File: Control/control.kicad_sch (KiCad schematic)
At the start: 0 parts

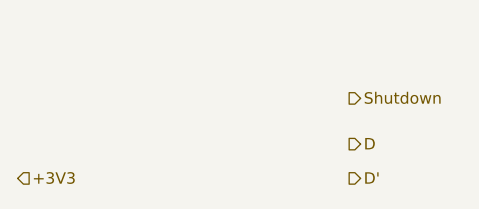
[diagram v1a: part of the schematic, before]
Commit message: added symbol libraries and finished gate driver circuitry schematic
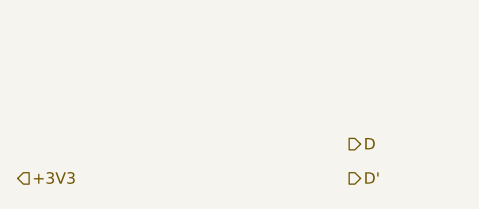
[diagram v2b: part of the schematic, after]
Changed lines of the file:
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@@
-		)
-	)
-	(hierarchical_label "Shutdown"
-		(shape output)
-		(at 176.53 90.17 0)
-		(effects
-			(font
-				(size 1.27 1.27)
-			)
-			(justify left)
 		)
 	)

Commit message: MSPM0 Connections
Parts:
- added J2-J4, J3-J1: Conn_01x10, Connector_PinSocket_2.54mm:PinSocket_2x10_P2.54mm_Vertical, symbol Connector_Generic:Conn_02x10_Odd_Even
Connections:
- net +3V3: now also J3-J1.1 (Pin_1)
- new net *D19: J2-J4.4 (Pin_4)
- new net *D37: J2-J4.7 (Pin_7)
- new net *D38: J2-J4.5 (Pin_5)
- new net *D39: J2-J4.3 (Pin_3)
- new net *D40: J2-J4.1 (Pin_1)
- new net +5V: J3-J1.2 (Pin_2)
- new net D10/SDA: J3-J1.19 (Pin_19)
- new net D11: J2-J4.20 (Pin_20)
- new net D12/SPI.CS: J2-J4.18 (Pin_18)
- new net D13/SPI.CS: J2-J4.16 (Pin_16)
- new net D14/SPI.MISO: J2-J4.14 (Pin_14)
- new net D15/SPI.MOSI: J2-J4.12 (Pin_12)
- new net D17: J2-J4.8 (Pin_8)
- new net D18/SPI.CS: J2-J4.6 (Pin_6)
- new net D23/ADC: J3-J1.6 (Pin_6)
- new net D24/ADC: J3-J1.8 (Pin_8)
- new net D25/ADC: J3-J1.10 (Pin_10)
- new net D26/ADC: J3-J1.12 (Pin_12)
- new net D27/ADC: J3-J1.14 (Pin_14)
- new net D28/ADC: J3-J1.16 (Pin_16)
- new net D29/DAC: J3-J1.18 (Pin_18)
- new net D2/ADC: J3-J1.3 (Pin_3)
- new net D30/DAC: J3-J1.20 (Pin_20)
- new net D31: J2-J4.19 (Pin_19)
- new net D32: J2-J4.17 (Pin_17)
- new net D33: J2-J4.15 (Pin_15)
- new net D34: J2-J4.13 (Pin_13)
- new net D35/TC: J2-J4.11 (Pin_11)
- new net D36/TC: J2-J4.9 (Pin_9)
- new net D3/UART.RX: J3-J1.5 (Pin_5)
- new net D4/UART.TX: J3-J1.7 (Pin_7)
- new net D5: J3-J1.9 (Pin_9)
- new net D6/ADC: J3-J1.11 (Pin_11)
- new net D7/SPI.CLK: J3-J1.13 (Pin_13)
- new net D8: J3-J1.15 (Pin_15)
- new net D9/SCL: J3-J1.17 (Pin_17)
- new net GND: J2-J4.2 (Pin_2), J3-J1.4 (Pin_4)
- new net RST/D16: J2-J4.10 (Pin_10)
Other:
- note added: "Distance between the two connection columns pins should be 1800 mil from the middle portion of the outer pins. Distance between the pins in the column is 100 mil."
- note added: "Page 5 of the documentation"
- note added: "Pin Schematics"

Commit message: Diff Amp
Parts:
- added R1, R2: 1000, Resistor_SMD:R_0603_1608Metric_Pad0.98x0.95mm_HandSolder, symbol Device:R_Small_US
- added R3, R4: 1100, Resistor_SMD:R_0603_1608Metric_Pad0.98x0.95mm_HandSolder, symbol Device:R_Small_US
- added U1: TLV2372, Package_SO:SOIC-8_3.9x4.9mm_P1.27mm, symbol Amplifier_Operational:TLV2372
- renumbered J2-J4 to J2-J?, J3-J1 to J3-J?
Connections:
- net +3V3: now also U1.8 (V+)
- net GND: now also R3.2, U1.4 (V-)
- new net: R2.2, R3.1, U1.2 (-)
- new net: R1.2, R4.1, U1.3 (+)
- new net V_{cap+}: R1.1
- new net V_{cap-}: R2.1
- new net Vout: R4.2, U1.1
- no-connect marks 0 -> 3
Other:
- note added: "Differential Amplifier V_{out}= 1.1(V_{cap-}-V_{cap+})"

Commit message: more simulation work + fixed some things in root schematic
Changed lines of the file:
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@@
 		)
 	)
-	(hierarchical_label "D"
+	(hierarchical_label "D1"
 		(shape output)
 		(at 176.53 95.25 0)
+		(effects
+			(font
+				(size 1.27 1.27)
+			)
+			(justify left)
+		)
+	)
+	(hierarchical_label "D2'"
+		(shape output)
+		(at 176.53 106.68 0)
 		(effects
 			(font
@@
 		)
 	)
-	(hierarchical_label "SCL_{IN}"
-		(shape input)
-		(at 161.29 95.25 180)
-		(effects
-			(font
-				(size 1.27 1.27)
-			)
-			(justify right)
-		)
-	)
 	(hierarchical_label "V_{cap-}"
 		(shape bidirectional)
@@
 		)
 	)
-	(hierarchical_label "SDA_{IN}"
-		(shape bidirectional)
-		(at 161.29 97.79 180)
-		(effects
-			(font
-				(size 1.27 1.27)
-			)
-			(justify right)
-		)
-	)
-	(hierarchical_label "D'"
+	(hierarchical_label "D1'"
 		(shape output)
 		(at 176.53 99.06 0)
@@
 		)
 	)
+	(hierarchical_label "D2"
+		(shape output)
+		(at 176.53 102.87 0)
+		(effects
+			(font
+				(size 1.27 1.27)
+			)
+			(justify left)
+		)
+	)

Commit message: wiring connected, now only need msmp0 pinout and footprint assignments
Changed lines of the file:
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@@
 	)
 	(hierarchical_label "V_{cap-}"
-		(shape bidirectional)
+		(shape input)
 		(at 118.11 77.47 180)
 		(effects
@@
 	)
 	(hierarchical_label "V_{cap+}"
-		(shape bidirectional)
+		(shape input)
 		(at 118.11 72.39 180)
 		(effects

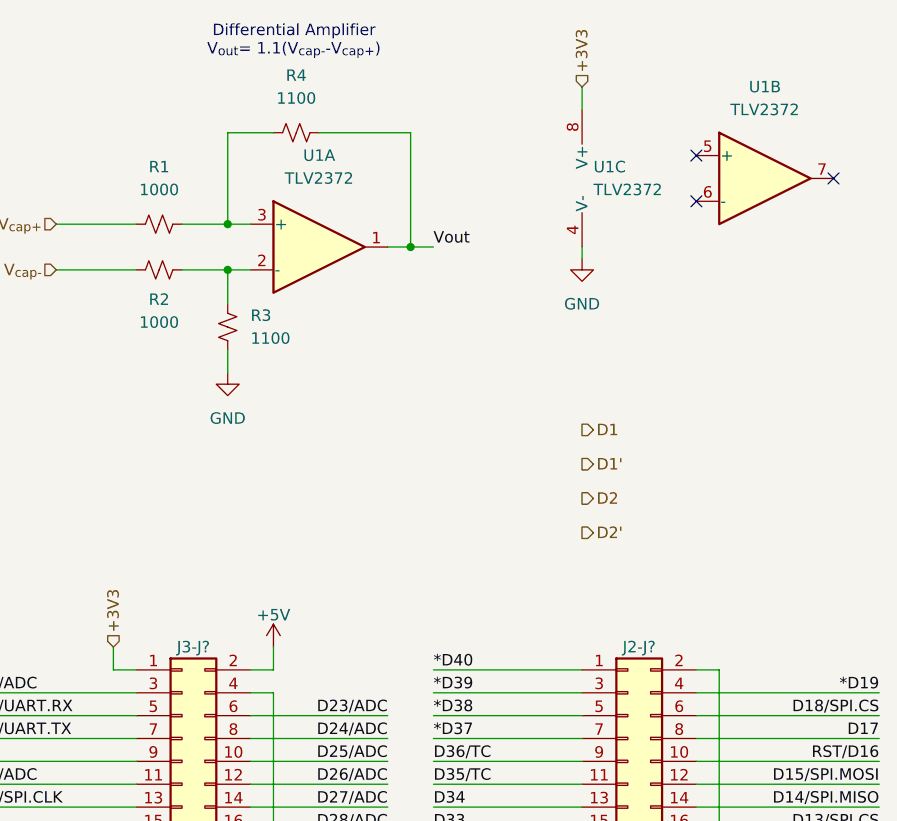
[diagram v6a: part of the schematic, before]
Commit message: removed v1 files and assigned mouser part numbers
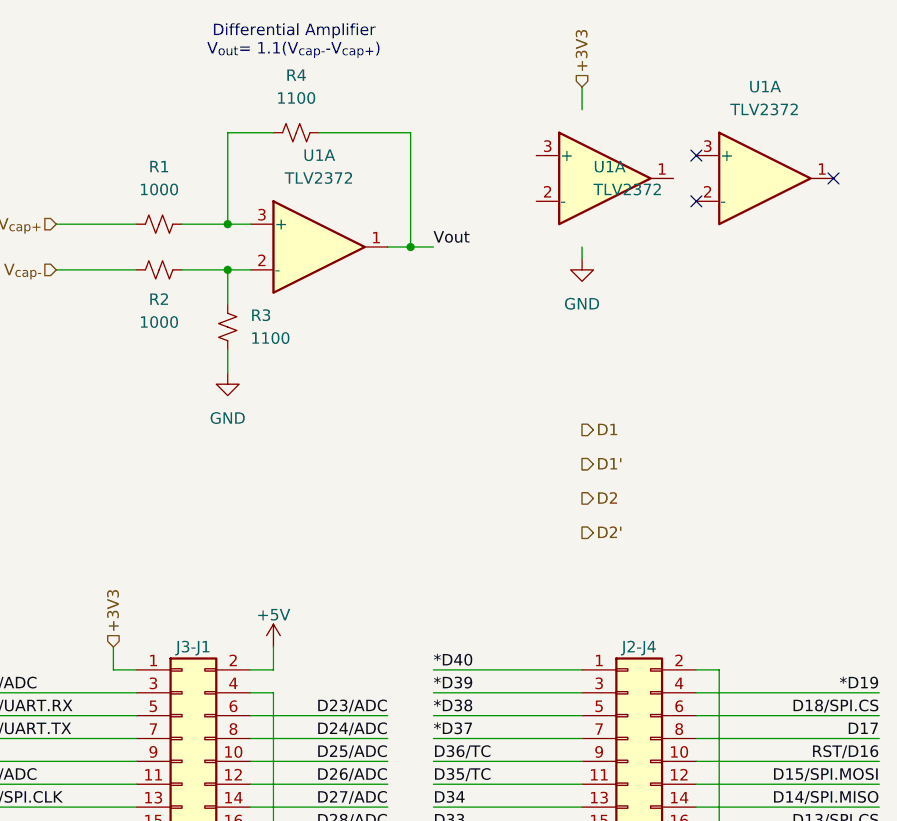
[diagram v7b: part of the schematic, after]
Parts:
- R1, R2: Manufacturer_Part_Number (none) -> RT0603DRD071KL; Mouser Part Number (none) -> 603-RT0603DRD071KL
- R3, R4: Manufacturer_Part_Number (none) -> RT0603DRD071K1L; Mouser Part Number (none) -> 603-RT0603DRD071K1L
- U1: now left out of the parts list
- gave numbers to parts that had none: 2
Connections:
- net +3V3: no longer U1.8 (V+)
- net GND: no longer U1.4 (V-)
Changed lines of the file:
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@@
 		(lib_id "Amplifier_Operational:TLV2372")
 		(at 196.85 67.31 0)
-		(unit 2)
-		(exclude_from_sim no)
-		(in_bom yes)
+		(unit 1)
+		(exclude_from_sim no)
+		(in_bom no)
 		(on_board yes)
 		(dnp no)
 		(fields_autoplaced yes)
-		(property "Reference" "U1"
+		(property "Reference" "U?"
 			(at 196.85 57.15 0)
 			(effects
@@
 				)
 			)
+			(project "control"
+				(path "/f194d5da-fd8d-4aa7-96f3-295d70bb8ae2"
+					(reference "U?")
+					(unit 1)
+				)
+			)
 		)
 	)
@@
 		(dnp no)
 		(fields_autoplaced yes)
-		(property "Reference" "R3"
+		(property "Reference" "R?"
 			(at 139.7 82.5499 0)
 			(effects
@@
 			)
 		)
-		(property "Datasheet" "~"
+		(property "Datasheet" "https://www.mouser.com/datasheet/3/508/1/PYu-RT_1-to-0.01_RoHS_L_15.pdf"
 			(at 137.16 83.82 0)
 			(effects
@@
 			)
 		)
+		(property "Manufacturer_Part_Number" "RT0603DRD071K1L"
+			(at 137.16 83.82 0)
+			(effects
+				(font
+					(size 1.27 1.27)
+				)
+				(hide yes)
+			)
+		)
+		(property "Mouser Part Number" "603-RT0603DRD071K1L"
+			(at 137.16 83.82 0)
+			(effects
+				(font
+					(size 1.27 1.27)
+				)
+				(hide yes)
+			)
+		)
 		(pin "1"
 		)
@@
 				(path "/98ee8313-37ab-4329-91ab-b5710476f82f/ee005c00-ec4f-437e-b20a-795d960ff7e7"
 					(reference "R3")
+					(unit 1)
+				)
+			)
+			(project "control"
+				(path "/f194d5da-fd8d-4aa7-96f3-295d70bb8ae2"
+					(reference "R?")
 					(unit 1)
 				)
@@
 		(on_board yes)
 		(dnp no)
-		(property "Reference" "#PWR?"
+		(property "Reference" "#PWR0103"
 			(at 142.24 153.67 0)
 			(effects
@@
 		(dnp no)
 		(fields_autoplaced yes)
-		(property "Reference" "#PWR05"
+		(property "Reference" "#PWR?"
 			(at 137.16 95.25 0)
 			(effects
@@
 				)
 			)
+			(project "control"
+				(path "/f194d5da-fd8d-4aa7-96f3-295d70bb8ae2"
+					(reference "#PWR?")
+					(unit 1)
+				)
+			)
 		)
 	)
@@
 		(on_board yes)
 		(dnp no)
-		(property "Reference" "R2"
+		(property "Reference" "R?"
 			(at 129.54 80.772 90)
 			(effects
@@
 			)
 		)
-		(property "Datasheet" "~"
+		(property "Datasheet" "https://www.mouser.com/datasheet/3/508/1/PYu-RT_1-to-0.01_RoHS_L_15.pdf"
 			(at 129.54 77.47 0)
 			(effects
@@
 			)
 		)
+		(property "Manufacturer_Part_Number" "RT0603DRD071KL"
+			(at 129.54 77.47 0)
+			(effects
+				(font
+					(size 1.27 1.27)
+				)
+				(hide yes)
+			)
+		)
+		(property "Mouser Part Number" "603-RT0603DRD071KL"
+			(at 129.54 77.47 0)
+			(effects
+				(font
+					(size 1.27 1.27)
+				)
+				(hide yes)
+			)
+		)
 		(pin "1"
 		)
@@
 				(path "/98ee8313-37ab-4329-91ab-b5710476f82f/ee005c00-ec4f-437e-b20a-795d960ff7e7"
 					(reference "R2")
+					(unit 1)
+				)
+			)
+			(project "control"
+				(path "/f194d5da-fd8d-4aa7-96f3-295d70bb8ae2"
+					(reference "R?")
 					(unit 1)
 				)
@@
 		(on_board yes)
 		(dnp no)
-		(property "Reference" "J3-J?"
+		(property "Reference" "J3-J1"
 			(at 133.35 119.38 0)
 			(effects
@@
 		(dnp no)
 		(fields_autoplaced yes)
-		(property "Reference" "R1"
+		(property "Reference" "R?"
 			(at 129.54 66.04 90)
 			(effects
@@
 			)
 		)
-		(property "Datasheet" "~"
+		(property "Datasheet" "https://www.mouser.com/datasheet/3/508/1/PYu-RT_1-to-0.01_RoHS_L_15.pdf"
 			(at 129.54 72.39 0)
 			(effects
@@
 			)
 		)
+		(property "Manufacturer_Part_Number" "RT0603DRD071KL"
+			(at 129.54 72.39 0)
+			(effects
+				(font
+					(size 1.27 1.27)
+				)
+				(hide yes)
+			)
+		)
+		(property "Mouser Part Number" "603-RT0603DRD071KL"
+			(at 129.54 72.39 0)
+			(effects
+				(font
+					(size 1.27 1.27)
+				)
+				(hide yes)
+			)
+		)
 		(pin "1"
 		)
@@
 				(path "/98ee8313-37ab-4329-91ab-b5710476f82f/ee005c00-ec4f-437e-b20a-795d960ff7e7"
 					(reference "R1")
+					(unit 1)
+				)
+			)
+			(project "control"
+				(path "/f194d5da-fd8d-4aa7-96f3-295d70bb8ae2"
+					(reference "R?")
 					(unit 1)
 				)
@@
 		(dnp no)
 		(fields_autoplaced yes)
-		(property "Reference" "#PWR013"
+		(property "Reference" "#PWR?"
 			(at 176.53 82.55 0)
 			(effects
@@
 				)
 			)
+			(project "control"
+				(path "/f194d5da-fd8d-4aa7-96f3-295d70bb8ae2"
+					(reference "#PWR?")
+					(unit 1)
+				)
+			)
 		)
 	)
@@
 		(unit 1)
 		(exclude_from_sim no)
-		(in_bom yes)
+		(in_bom no)
 		(on_board yes)
 		(dnp no)
 		(fields_autoplaced yes)
-		(property "Reference" "U1"
+		(property "Reference" "U?"
 			(at 147.32 64.77 0)
 			(effects
@@
 				)
 			)
+			(project "control"
+				(path "/f194d5da-fd8d-4aa7-96f3-295d70bb8ae2"
+					(reference "U?")
+					(unit 1)
+				)
+			)
 		)
 	)
@@
 		(on_board yes)
 		(dnp no)
-		(property "Reference" "J2-J?"
+		(property "Reference" "J2-J4"
 			(at 182.88 119.38 0)
 			(effects
@@
 		(lib_id "Amplifier_Operational:TLV2372")
 		(at 179.07 67.31 0)
-		(unit 3)
-		(exclude_from_sim no)
-		(in_bom yes)
+		(unit 1)
+		(exclude_from_sim no)
+		(in_bom no)
 		(on_board yes)
 		(dnp no)
 		(fields_autoplaced yes)
-		(property "Reference" "U1"
+		(property "Reference" "U?"
 			(at 177.8 66.0399 0)
 			(effects
@@
 				)
 			)
+			(project "control"
+				(path "/f194d5da-fd8d-4aa7-96f3-295d70bb8ae2"
+					(reference "U?")
+					(unit 1)
+				)
+			)
 		)
 	)
@@
 		(dnp no)
 		(fields_autoplaced yes)
-		(property "Reference" "R4"
+		(property "Reference" "R?"
 			(at 144.78 55.88 90)
 			(effects
@@
 			)
 		)
-		(property "Datasheet" "~"
+		(property "Datasheet" "https://www.mouser.com/datasheet/3/508/1/PYu-RT_1-to-0.01_RoHS_L_15.pdf"
 			(at 144.78 62.23 0)
 			(effects
@@
 			)
 		)
+		(property "Manufacturer_Part_Number" "RT0603DRD071K1L"
+			(at 144.78 62.23 0)
+			(effects
+				(font
+					(size 1.27 1.27)
+				)
+				(hide yes)
+			)
+		)
+		(property "Mouser Part Number" "603-RT0603DRD071K1L"
+			(at 144.78 62.23 0)
+			(effects
+				(font
+					(size 1.27 1.27)
+				)
+				(hide yes)
+			)
+		)
 		(pin "1"
 		)
@@
 				(path "/98ee8313-37ab-4329-91ab-b5710476f82f/ee005c00-ec4f-437e-b20a-795d960ff7e7"
 					(reference "R4")
+					(unit 1)
+				)
+			)
+			(project "control"
+				(path "/f194d5da-fd8d-4aa7-96f3-295d70bb8ae2"
+					(reference "R?")
 					(unit 1)
 				)
@@
 		(on_board yes)
 		(dnp no)
-		(property "Reference" "#PWR?"
+		(property "Reference" "#PWR0102"
 			(at 191.77 153.67 0)
 			(effects
@@
 		(on_board yes)
 		(dnp no)
-		(property "Reference" "#PWR?"
+		(property "Reference" "#PWR0104"
 			(at 142.24 123.19 0)
 			(effects

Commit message: began layout
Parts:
- added C_{smooth}1, C_{smooth}2, C_{smooth}3, C_{smooth}4: 4.7u, Capacitor_SMD:C_0805_2012Metric_Pad1.18x1.45mm_HandSolder, symbol Device:C
- added U2: ACS71240KEXBLT-050U5, Sensor_Current:Allegro_QFN-12-10-1EP_3x3mm_P0.5mm, symbol Sensor_Current:ACS711xEXLT-31AB
- added U3: ACS71240KEXBLT-010B3, Sensor_Current:Allegro_QFN-12-10-1EP_3x3mm_P0.5mm, symbol Sensor_Current:ACS711xEXLT-15AB
- renumbered J2-J4 to J2-J1
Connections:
- net +3V3: now also U1.8 (V+), C_{smooth}1.1, C_{smooth}2.1, C_{smooth}3.1, C_{smooth}4.1, U2.10 (VCC), U3.10 (VCC)
- net GND: now also U1.4 (V-), C_{smooth}1.2, C_{smooth}2.2, C_{smooth}3.2, C_{smooth}4.2, U2.3 (GND), U3.3 (GND)
- net V_{cap+} renamed V_{sc,+}
- net V_{sc,+}: now also U2.2 (IP-)
- net V_{cap-} renamed V_{sc,-}
- new net I_{L,out+}: U2.1 (IP+)
- new net I_{bat,in+}: U3.1 (IP+)
- new net I_{bat,out+}: U3.2 (IP-)
- no-connect marks 3 -> 11
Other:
- note added: "Battery Current Sensing"
- note added: "Capacitor Voltage Sensing"
- note added: "Click Here"
- note added: "Inductor Current Sensing"
- note added: "MSPM0G3507"
- note added: "Microcontroller"
- note added: "Notes: Distance between the two connection columns pins should be 1800 mil from the middle portion of the outer pins. Distance between the pins in the column is 100 mil."
- note added: "Pin Schematics: Documentation:"
- note removed: "Distance between the two connection columns pins should be 1800 mil from the middle portion of the outer pins. Distance between the pins in the column is 100 mil."
- note removed: "Page 5 of the documentation"
- note removed: "Pin Schematics"
- moved on the sheet: J2-J1, J3-J1, R1, R2, R3, R4, U1A, U1B
